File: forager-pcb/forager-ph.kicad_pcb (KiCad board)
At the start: 2 copper layers, 114.6 x 96.3 mm, 33 parts, among them J4 Conn_01x02_Pin

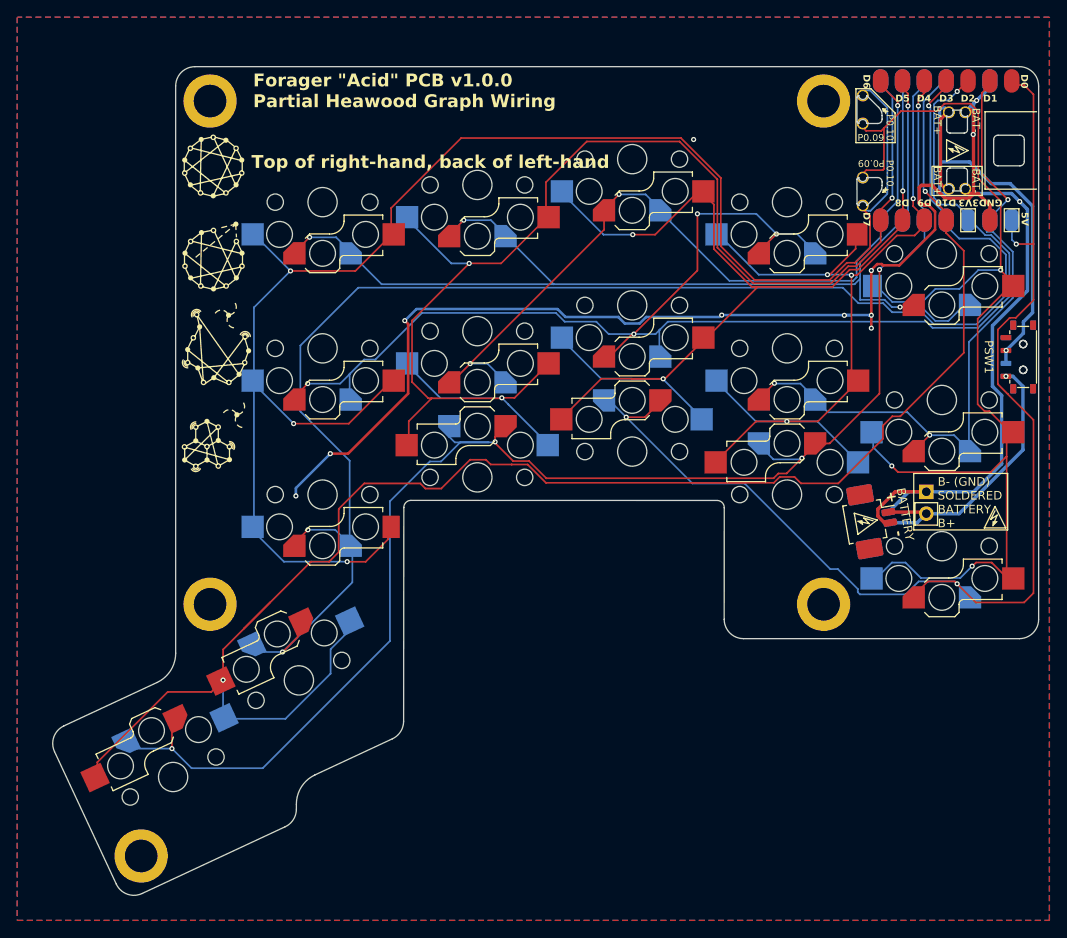
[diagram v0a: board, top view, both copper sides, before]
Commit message: Duplicate battery connectors with alternative polarity.
Also return to original's pads for the fall back battery soldering option.
The through holes seemed very small to me.

And update the version on the silksceen.
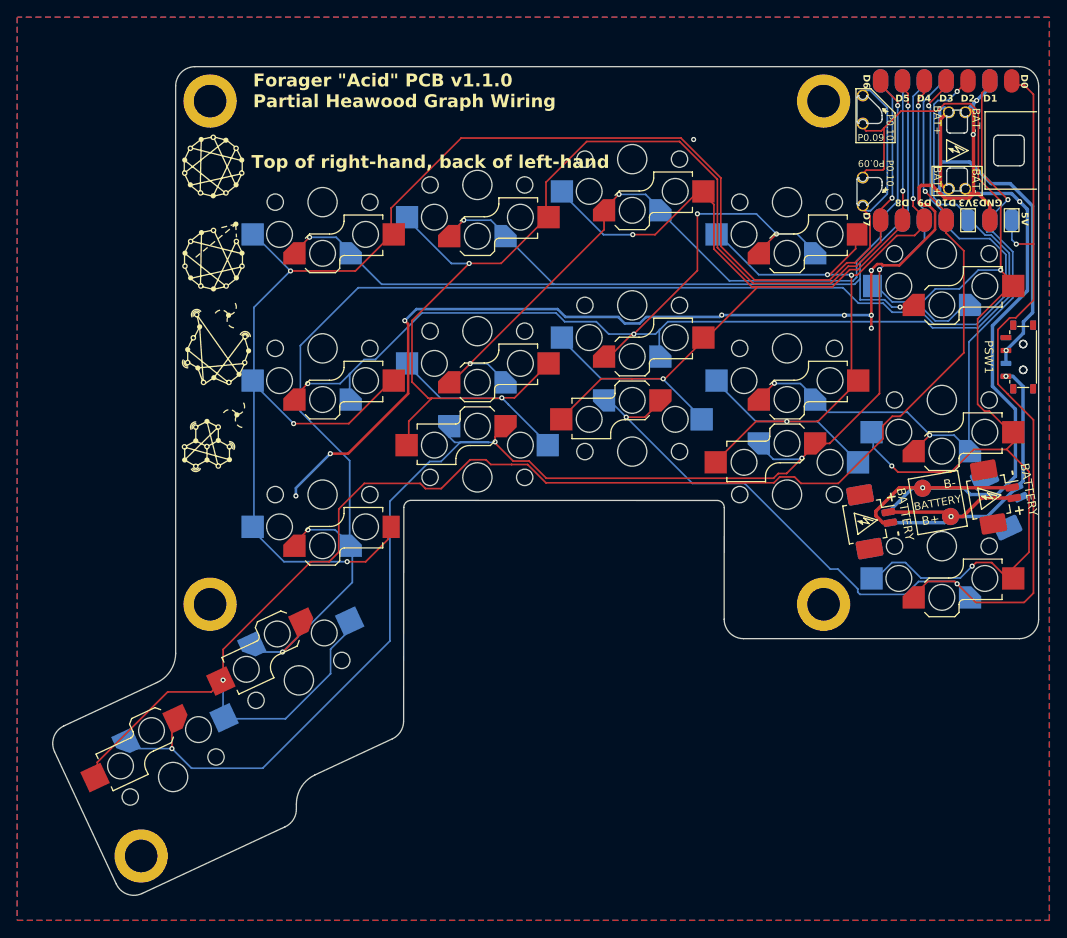
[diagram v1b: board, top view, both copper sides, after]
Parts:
- removed the ? at (111.9, 3.88)
- removed J4: Conn_01x02_Pin, Connector_PinHeader_2.54mm:PinHeader_1x02_P2.54mm_Vertical
- added ?: , clipboard:c6e4976e-07e6-4aae-98ea-2f932d7c0aa1, F.Cu at (111.2, -0.74)
- added ?: , , B.Cu at (104.8, -0.73)
- added ?: , clipboard:c6e4976e-07e6-4aae-98ea-2f932d7c0aa1, B.Cu at (112.7, 2.66)
- added ?: , , B.Cu at (108.0, 2.55)
- added BAT: Molex_PicoBlade_53261-0271_1x02-1MP_P1.25mm_Horizontal, Connector_Molex:Molex_PicoBlade_53261-0271_1x02-1MP_P1.25mm_Horizontal, B.Cu at (113.8, 0.75)
- added BATTERY: Molex_PicoBlade_53261-0271_1x02-1MP_P1.25mm_Horizontal, Connector_Molex:Molex_PicoBlade_53261-0271_1x02-1MP_P1.25mm_Horizontal, F.Cu at (112.9, 0.20)
- added TP3: TestPoint, TestPoint:TestPoint_Pad_D2.0mm, B.Cu at (108.0, 2.55)
- added TP4: TestPoint, TestPoint:TestPoint_Pad_D2.0mm, B.Cu at (104.8, -0.74)
- moved ? 21.8 mm to (135.8, 8.56)
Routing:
- net GND: track 199.6 -> 213.7 mm, vias 12 -> 13
- net BAT_CON: track 33.0 -> 45.8 mm, vias 1 -> 2
- net C5: track 192.9 -> 188.6 mm
- net C4: track 135.1 -> 138.4 mm
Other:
- board text added: "B+"
- board text added: "B-"
- board text added: "Forager {dblquote}Acid{dblquote} PCB v1.1.0 Partial Heawood Graph Wiring"
- board text removed: "(GND) B- SOLDERED BATTERY B+"
- board text removed: "B- (GND) SOLDERED BATTERY B+"
- board text removed: "Forager {dblquote}Acid{dblquote} PCB v1.0.0 Partial Heawood Graph Wiring"
